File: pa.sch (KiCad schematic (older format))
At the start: 10 parts

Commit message: Schematic finished
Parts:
- gave numbers to parts that had none: 10
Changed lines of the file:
@@
 LIBS:2450bl15b050
 LIBS:tlv4172
+LIBS:l4940d2t12-tr
+LIBS:tps54308
+LIBS:l78l33abu
+LIBS:adp150aujz-18
 LIBS:radar-cache
+LIBS:hn1c01fu
 EELAYER 25 0
 EELAYER END
 $Descr A4 11693 8268
 encoding utf-8
-Sheet 4 7
+Sheet 4 8
 Title ""
 Date ""
@@
 $EndDescr
 $Comp
-L QPA5219 U?
+L QPA5219 U401
 U 1 1 59D558DD
 P 5460 3360
-F 0 "U?" H 5960 2810 60  0000 C CNN
+F 0 "U401" H 5960 2810 60  0000 C CNN
 F 1 "QPA5219" H 5860 3860 60  0000 C CNN
 F 2 "" H 5410 3360 60  0001 C CNN
@@
 $EndComp
 $Comp
-L GND #PWR?
+L GND #PWR031
 U 1 1 59D559BE
 P 5460 4240
-F 0 "#PWR?" H 5460 3990 50  0001 C CNN
+F 0 "#PWR031" H 5460 3990 50  0001 C CNN
 F 1 "GND" H 5460 4090 50  0000 C CNN
 F 2 "" H 5460 4240 50  0001 C CNN
@@
 $EndComp
 $Comp
-L taper T?
+L taper T401
 U 1 1 59D55A9E
 P 6800 3310
-F 0 "T?" H 6800 3460 60  0000 C CNN
+F 0 "T401" H 6800 3460 60  0000 C CNN
 F 1 "taper" H 6700 3160 60  0000 C CNN
 F 2 "" H 6800 3310 60  0001 C CNN
@@
 $EndComp
 $Comp
-L taper T?
+L taper T402
 U 1 1 59D55B05
 P 4310 3360
-F 0 "T?" H 4310 3510 60  0000 C CNN
+F 0 "T402" H 4310 3510 60  0000 C CNN
 F 1 "taper" H 4210 3210 60  0000 C CNN
 F 2 "" H 4310 3360 60  0001 C CNN
@@
 $EndComp
 $Comp
-L C_Small C?
+L C_Small C404
 U 1 1 59D55C69
 P 6410 2470
-F 0 "C?" H 6420 2540 50  0000 L CNN
+F 0 "C404" H 6420 2540 50  0000 L CNN
 F 1 "0u1" H 6420 2390 50  0000 L CNN
 F 2 "" H 6410 2470 50  0001 C CNN
@@
 $EndComp
 $Comp
-L C_Small C?
+L C_Small C405
 U 1 1 59D55E73
 P 4810 2640
-F 0 "C?" H 4820 2710 50  0000 L CNN
+F 0 "C405" H 4820 2710 50  0000 L CNN
 F 1 "2u2" H 4820 2560 50  0000 L CNN
 F 2 "" H 4810 2640 50  0001 C CNN
@@
 $EndComp
 $Comp
-L C_Small C?
+L C_Small C401
 U 1 1 59D56103
 P 6410 1790
-F 0 "C?" H 6420 1860 50  0000 L CNN
+F 0 "C401" H 6420 1860 50  0000 L CNN
 F 1 "0u1" H 6420 1710 50  0000 L CNN
 F 2 "" H 6410 1790 50  0001 C CNN
@@
 $EndComp
 $Comp
-L C_Small C?
+L C_Small C402
 U 1 1 59D562A6
 P 6160 1800
-F 0 "C?" H 6170 1870 50  0000 L CNN
+F 0 "C402" H 6170 1870 50  0000 L CNN
 F 1 "2u2" H 6170 1720 50  0000 L CNN
 F 2 "" H 6160 1800 50  0001 C CNN
@@
 $EndComp
 $Comp
-L C_Small C?
+L C_Small C403
 U 1 1 59D5637B
 P 6150 2470
-F 0 "C?" H 6160 2540 50  0000 L CNN
+F 0 "C403" H 6160 2540 50  0000 L CNN
 F 1 "2u2" H 6160 2390 50  0000 L CNN
 F 2 "" H 6150 2470 50  0001 C CNN
@@
 $EndComp
 $Comp
-L GND #PWR?
+L GND #PWR032
 U 1 1 59D56500
 P 4810 2830
-F 0 "#PWR?" H 4810 2580 50  0001 C CNN
+F 0 "#PWR032" H 4810 2580 50  0001 C CNN
 F 1 "GND" H 4810 2680 50  0000 C CNN
 F 2 "" H 4810 2830 50  0001 C CNN
@@
 $EndComp
 $Comp
-L GND #PWR?
+L GND #PWR033
 U 1 1 59D5654D
 P 6410 1990
-F 0 "#PWR?" H 6410 1740 50  0001 C CNN
+F 0 "#PWR033" H 6410 1740 50  0001 C CNN
 F 1 "GND" H 6410 1840 50  0000 C CNN
 F 2 "" H 6410 1990 50  0001 C CNN
@@
 $EndComp
 $Comp
-L GND #PWR?
+L GND #PWR034
 U 1 1 59D56577
 P 6160 1990
-F 0 "#PWR?" H 6160 1740 50  0001 C CNN
+F 0 "#PWR034" H 6160 1740 50  0001 C CNN
 F 1 "GND" H 6160 1840 50  0000 C CNN
 F 2 "" H 6160 1990 50  0001 C CNN
@@
 $EndComp
 $Comp
-L GND #PWR?
+L GND #PWR035
 U 1 1 59D565EF
 P 6150 2670
-F 0 "#PWR?" H 6150 2420 50  0001 C CNN
+F 0 "#PWR035" H 6150 2420 50  0001 C CNN
 F 1 "GND" H 6150 2520 50  0000 C CNN
 F 2 "" H 6150 2670 50  0001 C CNN
@@
 $EndComp
 $Comp
-L GND #PWR?
+L GND #PWR036
 U 1 1 59D5663E
 P 6410 2680
-F 0 "#PWR?" H 6410 2430 50  0001 C CNN
+F 0 "#PWR036" H 6410 2430 50  0001 C CNN
 F 1 "GND" H 6410 2530 50  0000 C CNN
 F 2 "" H 6410 2680 50  0001 C CNN
@@
 EN
 $Comp
-L R_Small R?
+L R_Small R401
 U 1 1 59D56957
 P 4630 3090
-F 0 "R?" H 4660 3110 50  0000 L CNN
+F 0 "R401" H 4660 3110 50  0000 L CNN
 F 1 "10k" H 4660 3050 50  0000 L CNN
 F 2 "" H 4630 3090 50  0001 C CNN
@@
 Connection ~ 4630 3460
 $Comp
-L +3V3 #PWR?
+L +3V3 #PWR037
 U 1 1 59D56C8C
 P 4630 2890
-F 0 "#PWR?" H 4630 2740 50  0001 C CNN
+F 0 "#PWR037" H 4630 2740 50  0001 C CNN
 F 1 "+3V3" H 4630 3030 50  0000 C CNN
 F 2 "" H 4630 2890 50  0001 C CNN
@@
 	4630 2890 4630 2990
 $Comp
-L +5V #PWR?
+L +5V #PWR038
 U 1 1 59D56CE8
 P 4570 2270
-F 0 "#PWR?" H 4570 2120 50  0001 C CNN
+F 0 "#PWR038" H 4570 2120 50  0001 C CNN
 F 1 "+5V" H 4570 2410 50  0000 C CNN
 F 2 "" H 4570 2270 50  0001 C CNN
@@
 $EndComp
 $Comp
-L +5V #PWR?
+L +5V #PWR039
 U 1 1 59D56D15
 P 6510 1510
-F 0 "#PWR?" H 6510 1360 50  0001 C CNN
+F 0 "#PWR039" H 6510 1360 50  0001 C CNN
 F 1 "+5V" H 6510 1650 50  0000 C CNN
 F 2 "" H 6510 1510 50  0001 C CNN
@@
 $EndComp
 $Comp
-L +5V #PWR?
+L +5V #PWR040
 U 1 1 59D56D3B
 P 6610 2110
-F 0 "#PWR?" H 6610 1960 50  0001 C CNN
+F 0 "#PWR040" H 6610 1960 50  0001 C CNN
 F 1 "+5V" H 6610 2250 50  0000 C CNN
 F 2 "" H 6610 2110 50  0001 C CNN
@@
 Connection ~ 4810 2420
 $Comp
-L R_Small R?
+L R_Small R402
 U 1 1 59D57058
 P 6520 3810
-F 0 "R?" H 6550 3830 50  0000 L CNN
+F 0 "R402" H 6550 3830 50  0000 L CNN
 F 1 "27k" H 6550 3770 50  0000 L CNN
 F 2 "" H 6520 3810 50  0001 C CNN
@@
 	6520 3560 6520 3710
 $Comp
-L GND #PWR?
+L GND #PWR041
 U 1 1 59D572B3
 P 6520 4030
-F 0 "#PWR?" H 6520 3780 50  0001 C CNN
+F 0 "#PWR041" H 6520 3780 50  0001 C CNN
 F 1 "GND" H 6520 3880 50  0000 C CNN
 F 2 "" H 6520 4030 50  0001 C CNN

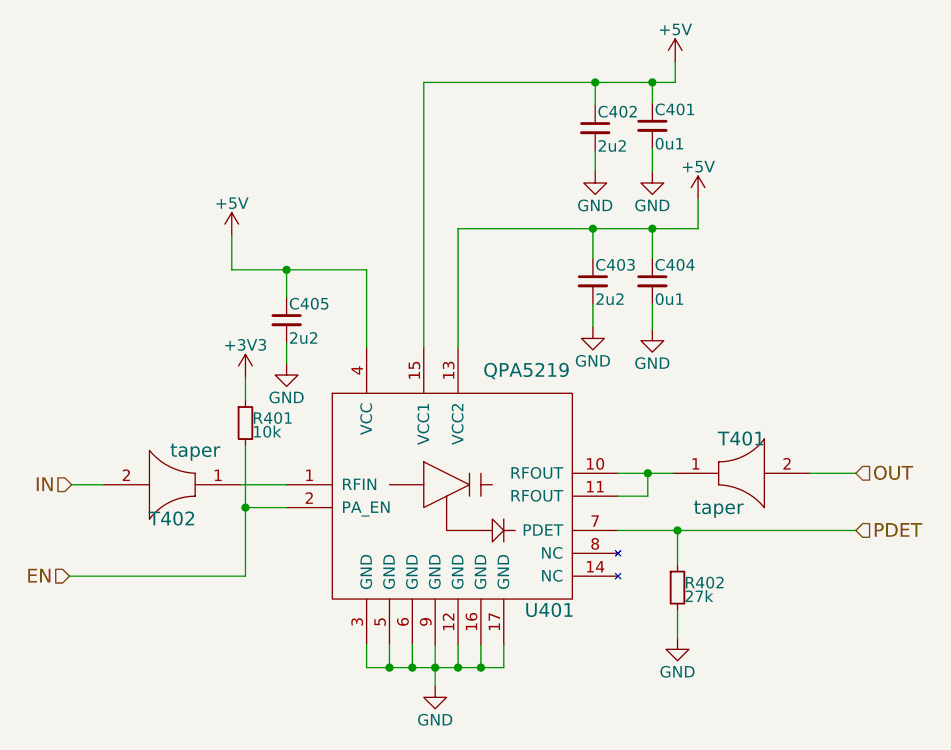
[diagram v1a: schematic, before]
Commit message: Assign a lot of footprints, fix l78l33abu part (input and output were reversed)
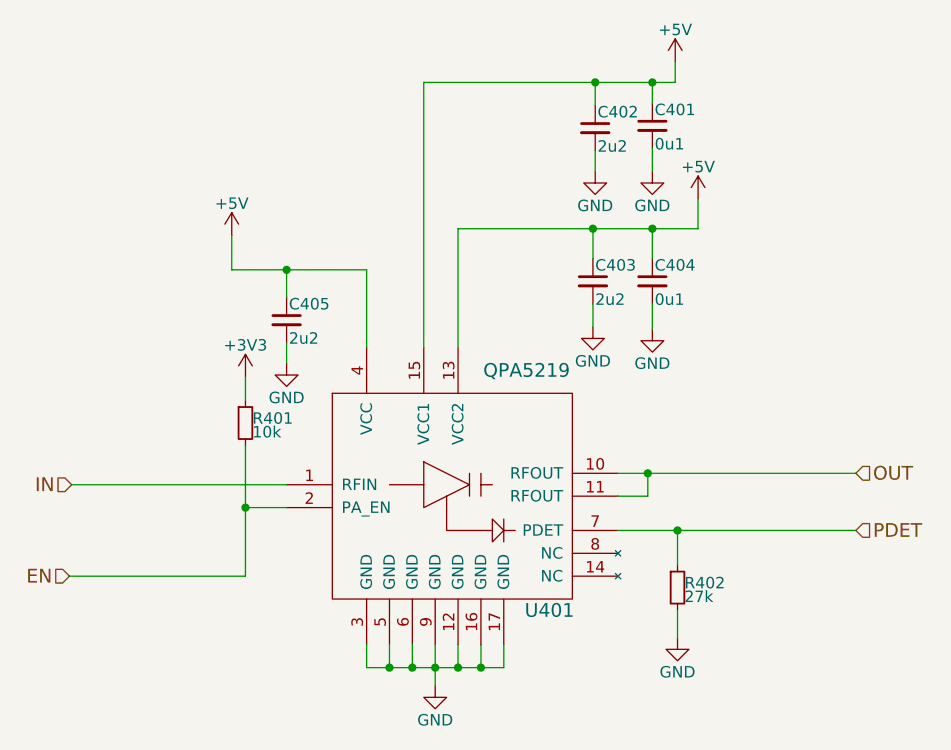
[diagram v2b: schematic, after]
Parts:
- removed T401, T402: taper, symbol taper
- C401, C404: footprint (none) -> Capacitors_SMD:C_0603_HandSoldering
- C402, C403, C405: footprint (none) -> Capacitors_SMD:C_0805_HandSoldering
- R401, R402: footprint (none) -> Resistors_SMD:R_0603_HandSoldering
- U401: footprint (none) -> rajsradar:QPA5219
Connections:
- net IN: now also U401.1 (RFIN)
- net OUT: now also U401.10 (RFOUT), U401.11 (RFOUT)
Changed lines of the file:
@@
 F 0 "U401" H 5960 2810 60  0000 C CNN
 F 1 "QPA5219" H 5860 3860 60  0000 C CNN
-F 2 "" H 5410 3360 60  0001 C CNN
+F 2 "rajsradar:QPA5219" H 5410 3360 60  0001 C CNN
 F 3 "" H 5410 3360 60  0001 C CNN
 	1    5460 3360
@@
 $EndComp
 $Comp
-L GND #PWR031
+L GND #PWR032
 U 1 1 59D559BE
 P 5460 4240
-F 0 "#PWR031" H 5460 3990 50  0001 C CNN
+F 0 "#PWR032" H 5460 3990 50  0001 C CNN
 F 1 "GND" H 5460 4090 50  0000 C CNN
 F 2 "" H 5460 4240 50  0001 C CNN
@@
 	1    5460 4240
 	1    0    0    -1
-$EndComp
-$Comp
-L taper T401
-U 1 1 59D55A9E
-P 6800 3310
-F 0 "T401" H 6800 3460 60  0000 C CNN
-F 1 "taper" H 6700 3160 60  0000 C CNN
-F 2 "" H 6800 3310 60  0001 C CNN
-F 3 "" H 6800 3310 60  0001 C CNN
-	1    6800 3310
-	1    0    0    -1
-$EndComp
-$Comp
-L taper T402
-U 1 1 59D55B05
-P 4310 3360
-F 0 "T402" H 4310 3510 60  0000 C CNN
-F 1 "taper" H 4210 3210 60  0000 C CNN
-F 2 "" H 4310 3360 60  0001 C CNN
-F 3 "" H 4310 3360 60  0001 C CNN
-	1    4310 3360
-	-1   0    0    1
 $EndComp
 $Comp
@@
 F 0 "C404" H 6420 2540 50  0000 L CNN
 F 1 "0u1" H 6420 2390 50  0000 L CNN
-F 2 "" H 6410 2470 50  0001 C CNN
+F 2 "Capacitors_SMD:C_0603_HandSoldering" H 6410 2470 50  0001 C CNN
 F 3 "" H 6410 2470 50  0001 C CNN
 	1    6410 2470
@@
 F 0 "C405" H 4820 2710 50  0000 L CNN
 F 1 "2u2" H 4820 2560 50  0000 L CNN
-F 2 "" H 4810 2640 50  0001 C CNN
+F 2 "Capacitors_SMD:C_0805_HandSoldering" H 4810 2640 50  0001 C CNN
 F 3 "" H 4810 2640 50  0001 C CNN
 	1    4810 2640
@@
 F 0 "C401" H 6420 1860 50  0000 L CNN
 F 1 "0u1" H 6420 1710 50  0000 L CNN
-F 2 "" H 6410 1790 50  0001 C CNN
+F 2 "Capacitors_SMD:C_0603_HandSoldering" H 6410 1790 50  0001 C CNN
 F 3 "" H 6410 1790 50  0001 C CNN
 	1    6410 1790
@@
 F 0 "C402" H 6170 1870 50  0000 L CNN
 F 1 "2u2" H 6170 1720 50  0000 L CNN
-F 2 "" H 6160 1800 50  0001 C CNN
+F 2 "Capacitors_SMD:C_0805_HandSoldering" H 6160 1800 50  0001 C CNN
 F 3 "" H 6160 1800 50  0001 C CNN
 	1    6160 1800
@@
 F 0 "C403" H 6160 2540 50  0000 L CNN
 F 1 "2u2" H 6160 2390 50  0000 L CNN
-F 2 "" H 6150 2470 50  0001 C CNN
+F 2 "Capacitors_SMD:C_0805_HandSoldering" H 6150 2470 50  0001 C CNN
 F 3 "" H 6150 2470 50  0001 C CNN
 	1    6150 2470
@@
 $EndComp
 $Comp
-L GND #PWR032
+L GND #PWR033
 U 1 1 59D56500
 P 4810 2830
-F 0 "#PWR032" H 4810 2580 50  0001 C CNN
+F 0 "#PWR033" H 4810 2580 50  0001 C CNN
 F 1 "GND" H 4810 2680 50  0000 C CNN
 F 2 "" H 4810 2830 50  0001 C CNN
@@
 $EndComp
 $Comp
-L GND #PWR033
+L GND #PWR034
 U 1 1 59D5654D
 P 6410 1990
-F 0 "#PWR033" H 6410 1740 50  0001 C CNN
+F 0 "#PWR034" H 6410 1740 50  0001 C CNN
 F 1 "GND" H 6410 1840 50  0000 C CNN
 F 2 "" H 6410 1990 50  0001 C CNN
@@
 $EndComp
 $Comp
-L GND #PWR034
+L GND #PWR035
 U 1 1 59D56577
 P 6160 1990
-F 0 "#PWR034" H 6160 1740 50  0001 C CNN
+F 0 "#PWR035" H 6160 1740 50  0001 C CNN
 F 1 "GND" H 6160 1840 50  0000 C CNN
 F 2 "" H 6160 1990 50  0001 C CNN
@@
 $EndComp
 $Comp
-L GND #PWR035
+L GND #PWR036
 U 1 1 59D565EF
 P 6150 2670
-F 0 "#PWR035" H 6150 2420 50  0001 C CNN
+F 0 "#PWR036" H 6150 2420 50  0001 C CNN
 F 1 "GND" H 6150 2520 50  0000 C CNN
 F 2 "" H 6150 2670 50  0001 C CNN
@@
 $EndComp
 $Comp
-L GND #PWR036
+L GND #PWR037
 U 1 1 59D5663E
 P 6410 2680
-F 0 "#PWR036" H 6410 2430 50  0001 C CNN
+F 0 "#PWR037" H 6410 2430 50  0001 C CNN
 F 1 "GND" H 6410 2530 50  0000 C CNN
 F 2 "" H 6410 2680 50  0001 C CNN
@@
 F 0 "R401" H 4660 3110 50  0000 L CNN
 F 1 "10k" H 4660 3050 50  0000 L CNN
-F 2 "" H 4630 3090 50  0001 C CNN
+F 2 "Resistors_SMD:R_0603_HandSoldering" H 4630 3090 50  0001 C CNN
 F 3 "" H 4630 3090 50  0001 C CNN
 	1    4630 3090
@@
 Connection ~ 5260 4160
 Wire Wire Line
-	4610 3360 4810 3360
-Wire Wire Line
-	6500 3310 6260 3310
+	3870 3360 4810 3360
+Wire Wire Line
+	6260 3310 7300 3310
 Wire Wire Line
 	6260 3410 6390 3410
@@
 	6410 2680 6410 2570
 Wire Wire Line
-	3870 3360 4010 3360
-Wire Wire Line
-	7300 3310 7100 3310
-Wire Wire Line
 	4630 3760 3860 3760
 Wire Wire Line
@@
 Connection ~ 4630 3460
 $Comp
-L +3V3 #PWR037
+L +3V3 #PWR038
 U 1 1 59D56C8C
 P 4630 2890
-F 0 "#PWR037" H 4630 2740 50  0001 C CNN
+F 0 "#PWR038" H 4630 2740 50  0001 C CNN
 F 1 "+3V3" H 4630 3030 50  0000 C CNN
 F 2 "" H 4630 2890 50  0001 C CNN
@@
 	4630 2890 4630 2990
 $Comp
-L +5V #PWR038
+L +5V #PWR039
 U 1 1 59D56CE8
 P 4570 2270
-F 0 "#PWR038" H 4570 2120 50  0001 C CNN
+F 0 "#PWR039" H 4570 2120 50  0001 C CNN
 F 1 "+5V" H 4570 2410 50  0000 C CNN
 F 2 "" H 4570 2270 50  0001 C CNN
@@
 $EndComp
 $Comp
-L +5V #PWR039
+L +5V #PWR040
 U 1 1 59D56D15
 P 6510 1510
-F 0 "#PWR039" H 6510 1360 50  0001 C CNN
+F 0 "#PWR040" H 6510 1360 50  0001 C CNN
 F 1 "+5V" H 6510 1650 50  0000 C CNN
 F 2 "" H 6510 1510 50  0001 C CNN
@@
 $EndComp
 $Comp
-L +5V #PWR040
+L +5V #PWR041
 U 1 1 59D56D3B
 P 6610 2110
-F 0 "#PWR040" H 6610 1960 50  0001 C CNN
+F 0 "#PWR041" H 6610 1960 50  0001 C CNN
 F 1 "+5V" H 6610 2250 50  0000 C CNN
 F 2 "" H 6610 2110 50  0001 C CNN
@@
 F 0 "R402" H 6550 3830 50  0000 L CNN
 F 1 "27k" H 6550 3770 50  0000 L CNN
-F 2 "" H 6520 3810 50  0001 C CNN
+F 2 "Resistors_SMD:R_0603_HandSoldering" H 6520 3810 50  0001 C CNN
 F 3 "" H 6520 3810 50  0001 C CNN
 	1    6520 3810
@@
 	6520 3560 6520 3710
 $Comp
-L GND #PWR041
+L GND #PWR042
 U 1 1 59D572B3
 P 6520 4030
-F 0 "#PWR041" H 6520 3780 50  0001 C CNN
+F 0 "#PWR042" H 6520 3780 50  0001 C CNN
 F 1 "GND" H 6520 3880 50  0000 C CNN
 F 2 "" H 6520 4030 50  0001 C CNN
